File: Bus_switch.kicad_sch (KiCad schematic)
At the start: 7 parts, among them J3 Conn_01x04_Pin, U1 SN74CB3Q3384APW

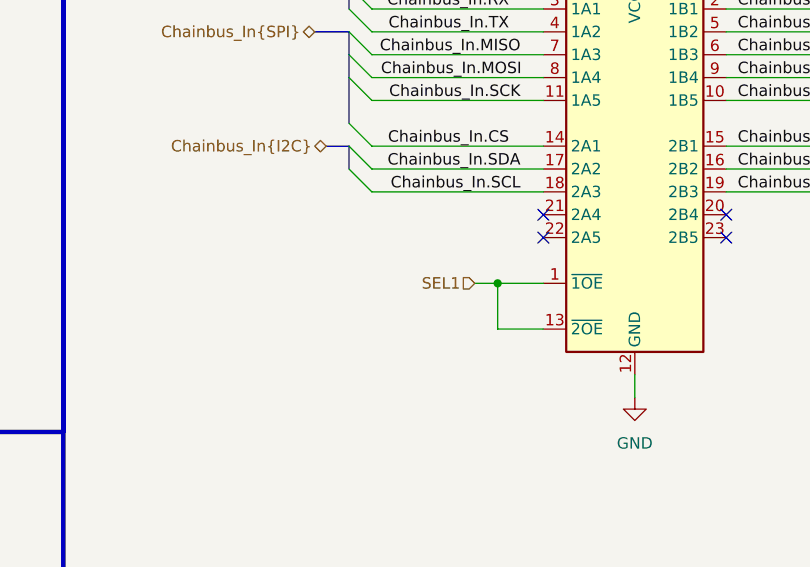
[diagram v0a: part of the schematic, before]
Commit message: added pullup on bus switch negate OE
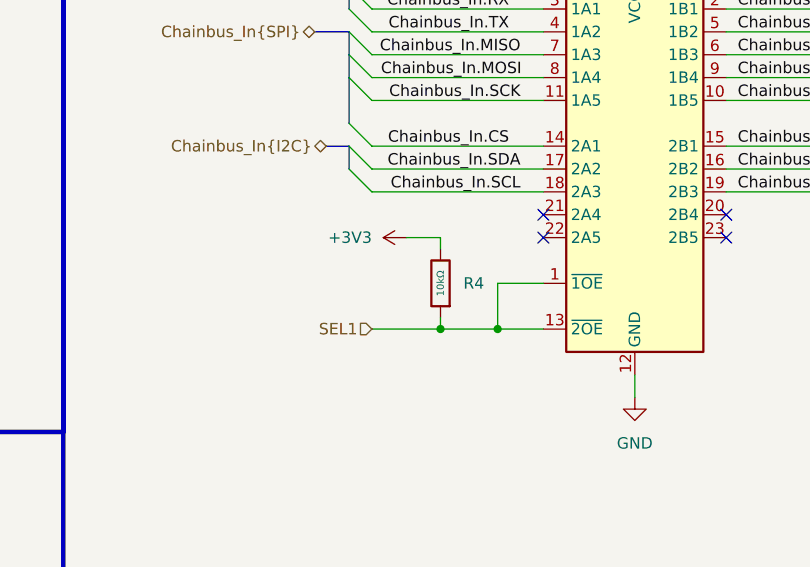
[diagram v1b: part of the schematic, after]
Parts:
- added R4: 10kΩ, PCM_JLCPCB:R_0402, symbol PCM_JLCPCB-Resistors:0402,10kΩ
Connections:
- net +3V3: now also R4.2
- net SEL1: now also R4.1

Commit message: moved I2C header to the side
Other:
- title: MMS3 Stepper Controler -> MMS3 Hat template small (Change Me)
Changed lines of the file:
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@@
 	(paper "A4")
 	(title_block
-		(title "MMS3 Stepper Controler")
+		(title "MMS3 Hat template small (Change Me)")
 		(date "2026-02-25")
-		(rev "R0")
+		(rev "A")
 		(comment 1 "Made by Wojciech Szafrański")
 		(comment 2 "Designed in poland")
-		(comment 3 "MMS3 Hat based on Chainbus")
 	)
 	(rectangle
